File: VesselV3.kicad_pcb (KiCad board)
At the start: 2 copper layers, 0 parts

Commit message: PCB layout - Initial Commit
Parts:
- added BuckConverter1v8: TPS6285010MQDRLRQ1, SamacSys_Parts:SOTFL50P160X60-8N, F.Cu at (281.0, 51.8)
- added BuckConverter3v3: AP63203WU-7, SamacSys_Parts:SOT95P280X100-6N, F.Cu at (235.4, 45.8)
- added C1: 20pF, SamacSys_Parts:C0805, F.Cu at (199.1, 56.1)
- added C10: 4.7u, SamacSys_Parts:C0805, F.Cu at (378.3, 112.7)
- added C11: 4.7u, SamacSys_Parts:C0805, F.Cu at (378.3, 134.5)
- added C12: 4.7u, SamacSys_Parts:C0805, F.Cu at (378.3, 153.4)
- added C13: 4.7u, SamacSys_Parts:C0805, F.Cu at (378.3, 172.5)
- added C14: 4.7u, SamacSys_Parts:C0805, F.Cu at (378.3, 191.5)
- added C15: 4.7u, SamacSys_Parts:C0805, F.Cu at (354.8, 194.3)
- added C16: 2.2uF, SamacSys_Parts:CAPC1608X90N, F.Cu at (272.2, 65.8)
- added C17: 0.1uF, SamacSys_Parts:CAPC1005X55N, F.Cu at (265.8, 60.1)
- added C18: 4.7u, SamacSys_Parts:C0805, F.Cu at (342.7, 41.0)
- added C19: c=1e-05, SamacSys_Parts:CAPC2012X140N, F.Cu at (285.8, 49.3)
- added C2: 20pF, SamacSys_Parts:C0805, F.Cu at (213.3, 70.3)
- added C20: c=1e-05, SamacSys_Parts:CAPC2012X140N, F.Cu at (287.8, 49.3)
- added C21: 10pF, SamacSys_Parts:CAPC2012X75N, F.Cu at (277.1, 54.5)
- added C22: c=1e-05, SamacSys_Parts:CAPC2012X140N, F.Cu at (275.5, 59.2)
- added C23: c=1e-05, SamacSys_Parts:CAPC2012X140N, F.Cu at (279.0, 59.2)
- added C24: 0.1uF, SamacSys_Parts:CAPC1005X55N, F.Cu at (267.0, 60.1)
- added C25: 0.1uF, SamacSys_Parts:CAPC1005X55N, F.Cu at (211.0, 63.4)
- added C26: 0.1uF, SamacSys_Parts:CAPC1005X55N, F.Cu at (207.6, 52.3)
- added C27: 0.1uF, SamacSys_Parts:CAPC1005X55N, F.Cu at (227.0, 58.6)
- added C28: 0.1uF, SamacSys_Parts:CAPC1005X55N, F.Cu at (219.1, 46.4)
- added C29: 4.7u, SamacSys_Parts:C0805, F.Cu at (224.3, 61.2)
- added C3: 0.1u, SamacSys_Parts:C0805, F.Cu at (202.4, 52.2)
- added C30: 0.1uF, SamacSys_Parts:CAPC1005X55N, F.Cu at (210.3, 61.1)
- added C31: 0.1uF, SamacSys_Parts:CAPC1005X55N, F.Cu at (221.4, 64.0)
- added C32: 0.1uF, SamacSys_Parts:CAPC1005X55N, F.Cu at (299.7, 50.0)
- added C33: c=1e-05, SamacSys_Parts:CAPC2012X140N, F.Cu at (293.1, 51.9)
- added C34: 0.1uF, SamacSys_Parts:CAPC1005X55N, F.Cu at (272.2, 63.6)
- added C35: 2.2uF, SamacSys_Parts:CAPC1608X90N, F.Cu at (281.8, 64.1)
- added C36: 0.01u, SamacSys_Parts:CAPC1005X56N, F.Cu at (201.0, 41.3)
- added C37: 0.01u, SamacSys_Parts:CAPC1005X56N, F.Cu at (200.2, 42.1)
- added C38: 0.1uF, SamacSys_Parts:CAPC1005X55N, F.Cu at (204.8, 49.8)
- added C39: 0.1uF, SamacSys_Parts:CAPC1005X55N, F.Cu at (200.5, 45.5)
- added C4: c=2.2e-05, SamacSys_Parts:CAPC2012X95N, F.Cu at (236.7, 59.6)
- added C40: 0.1uF, SamacSys_Parts:CAPC1005X55N, F.Cu at (268.2, 60.1)
- added C41: 0.01u, SamacSys_Parts:CAPC1005X56N, F.Cu at (201.8, 40.7)
- added C5: c=2.2e-05, SamacSys_Parts:CAPC2012X95N, F.Cu at (236.7, 61.6)
- added C6: c=1e-07, SamacSys_Parts:CAPC2012X95N, F.Cu at (236.0, 50.9)
- added C7: c=1e-05, SamacSys_Parts:CAPC2012X140N, F.Cu at (235.1, 42.2)
- added C8: 0.1u, SamacSys_Parts:C0805, F.Cu at (220.8, 39.4)
- added C9: 4.7u, SamacSys_Parts:C0805, F.Cu at (378.3, 90.8)
- added D1: D_Small, SamacSys_Parts:SODFL3816X120N, B.Cu at (62.5, 90.5)
- added D10: D_Small, SamacSys_Parts:SODFL3816X120N, B.Cu at (253.0, 90.5)
- added D100: D_Small, SamacSys_Parts:SODFL3816X120N, B.Cu at (310.2, 210.5)
- added D101: D_Small, SamacSys_Parts:SODFL3816X120N, B.Cu at (329.2, 210.5)
- added D102: D_Small, SamacSys_Parts:SODFL3816X120N, B.Cu at (348.3, 210.5)
- added D11: D_Small, SamacSys_Parts:SODFL3816X120N, B.Cu at (276.9, 90.5)
- added D12: D_Small, SamacSys_Parts:SODFL3816X120N, B.Cu at (295.9, 90.5)
- added D13: D_Small, SamacSys_Parts:SODFL3816X120N, B.Cu at (334.0, 90.5)
- added D14: D_Small, SamacSys_Parts:SODFL3816X120N, B.Cu at (353.1, 90.5)
- added D15: D_Small, SamacSys_Parts:SODFL3816X120N, B.Cu at (372.1, 90.5)
- added D16: D_Small, SamacSys_Parts:SODFL3816X120N, B.Cu at (62.5, 112.4)
- added D17: D_Small, SamacSys_Parts:SODFL3816X120N, B.Cu at (91.1, 112.4)
- added D18: D_Small, SamacSys_Parts:SODFL3816X120N, B.Cu at (110.2, 112.4)
- added D19: D_Small, SamacSys_Parts:SODFL3816X120N, B.Cu at (129.2, 112.4)
- added D2: D_Small, SamacSys_Parts:SODFL3816X120N, B.Cu at (81.6, 90.5)
- added D20: D_Small, SamacSys_Parts:SODFL3816X120N, B.Cu at (148.3, 112.4)
- added D21: D_Small, SamacSys_Parts:SODFL3816X120N, B.Cu at (172.1, 112.4)
- added D22: D_Small, SamacSys_Parts:SODFL3816X120N, B.Cu at (191.1, 112.4)
- added D23: D_Small, SamacSys_Parts:SODFL3816X120N, B.Cu at (210.2, 112.4)
- added D24: D_Small, SamacSys_Parts:SODFL3816X120N, B.Cu at (229.2, 112.4)
- added D25: D_Small, SamacSys_Parts:SODFL3816X120N, B.Cu at (253.0, 112.4)
- added D26: D_Small, SamacSys_Parts:SODFL3816X120N, B.Cu at (272.1, 112.4)
- added D27: D_Small, SamacSys_Parts:SODFL3816X120N, B.Cu at (291.1, 112.4)
- added D28: D_Small, SamacSys_Parts:SODFL3816X120N, B.Cu at (310.2, 112.4)
- added D29: D_Small, SamacSys_Parts:SODFL3816X120N, B.Cu at (334.0, 112.4)
- added D3: D_Small, SamacSys_Parts:SODFL3816X120N, B.Cu at (105.4, 90.5)
- added D30: D_Small, SamacSys_Parts:SODFL3816X120N, B.Cu at (353.1, 112.4)
- added D31: D_Small, SamacSys_Parts:SODFL3816X120N, B.Cu at (372.1, 112.4)
- added D32: D_Small, SamacSys_Parts:SODFL3816X120N, B.Cu at (62.5, 134.3)
- added D33: D_Small, SamacSys_Parts:SODFL3816X120N, B.Cu at (81.6, 134.3)
- added D34: D_Small, SamacSys_Parts:SODFL3816X120N, B.Cu at (100.6, 134.3)
- added D35: D_Small, SamacSys_Parts:SODFL3816X120N, B.Cu at (119.7, 134.3)
- added D36: D_Small, SamacSys_Parts:SODFL3816X120N, B.Cu at (138.7, 134.3)
- added D37: D_Small, SamacSys_Parts:SODFL3816X120N, B.Cu at (157.8, 134.3)
- added D38: D_Small, SamacSys_Parts:SODFL3816X120N, B.Cu at (176.8, 134.3)
- added D39: D_Small, SamacSys_Parts:SODFL3816X120N, B.Cu at (195.9, 134.3)
- added D4: D_Small, SamacSys_Parts:SODFL3816X120N, B.Cu at (124.5, 90.5)
- added D40: D_Small, SamacSys_Parts:SODFL3816X120N, B.Cu at (214.9, 134.3)
- added D41: D_Small, SamacSys_Parts:SODFL3816X120N, B.Cu at (234.0, 134.3)
- added D42: D_Small, SamacSys_Parts:SODFL3816X120N, B.Cu at (253.0, 134.3)
- added D43: D_Small, SamacSys_Parts:SODFL3816X120N, B.Cu at (272.1, 134.3)
- added D44: D_Small, SamacSys_Parts:SODFL3816X120N, B.Cu at (291.1, 134.3)
- added D45: D_Small, SamacSys_Parts:SODFL3816X120N, B.Cu at (319.7, 134.3)
- added D46: D_Small, SamacSys_Parts:SODFL3816X120N, B.Cu at (353.1, 134.3)
- added D47: D_Small, SamacSys_Parts:SODFL3816X120N, B.Cu at (372.1, 134.3)
- added D48: D_Small, SamacSys_Parts:SODFL3816X120N, B.Cu at (67.3, 153.3)
- added D49: D_Small, SamacSys_Parts:SODFL3816X120N, B.Cu at (91.1, 153.3)
- added D5: D_Small, SamacSys_Parts:SODFL3816X120N, B.Cu at (148.3, 90.5)
- added D50: D_Small, SamacSys_Parts:SODFL3816X120N, B.Cu at (110.2, 153.3)
- added D51: D_Small, SamacSys_Parts:SODFL3816X120N, B.Cu at (129.2, 153.3)
- added D52: D_Small, SamacSys_Parts:SODFL3816X120N, B.Cu at (148.3, 153.3)
- added D53: D_Small, SamacSys_Parts:SODFL3816X120N, B.Cu at (167.3, 153.3)
- added D54: D_Small, SamacSys_Parts:SODFL3816X120N, B.Cu at (186.4, 153.3)
- added D55: D_Small, SamacSys_Parts:SODFL3816X120N, B.Cu at (205.4, 153.3)
- added D56: D_Small, SamacSys_Parts:SODFL3816X120N, B.Cu at (224.5, 153.3)
- added D57: D_Small, SamacSys_Parts:SODFL3816X120N, B.Cu at (243.5, 153.3)
- added D58: D_Small, SamacSys_Parts:SODFL3816X120N, B.Cu at (262.6, 153.3)
- added D59: D_Small, SamacSys_Parts:SODFL3816X120N, B.Cu at (281.6, 153.3)
- added D6: D_Small, SamacSys_Parts:SODFL3816X120N, B.Cu at (167.3, 90.5)
- added D60: D_Small, SamacSys_Parts:SODFL3816X120N, B.Cu at (300.7, 153.3)
- added D61: D_Small, SamacSys_Parts:SODFL3816X120N, B.Cu at (326.9, 162.8)
- added D62: D_Small, SamacSys_Parts:SODFL3816X120N, B.Cu at (353.1, 153.3)
- added D63: D_Small, SamacSys_Parts:SODFL3816X120N, B.Cu at (372.1, 153.3)
- added D64: D_Small, SamacSys_Parts:SODFL3816X120N, B.Cu at (69.7, 172.4)
- added D65: D_Small, SamacSys_Parts:SODFL3816X120N, B.Cu at (95.9, 172.4)
- added D66: D_Small, SamacSys_Parts:SODFL3816X120N, B.Cu at (114.9, 172.4)
- added D67: D_Small, SamacSys_Parts:SODFL3816X120N, B.Cu at (134.0, 172.4)
- added D68: D_Small, SamacSys_Parts:SODFL3816X120N, B.Cu at (153.0, 172.4)
- added D69: D_Small, SamacSys_Parts:SODFL3816X120N, B.Cu at (172.1, 172.4)
- added D7: D_Small, SamacSys_Parts:SODFL3816X120N, B.Cu at (191.1, 90.5)
- added D70: D_Small, SamacSys_Parts:SODFL3816X120N, B.Cu at (191.1, 172.4)
- added D71: D_Small, SamacSys_Parts:SODFL3816X120N, B.Cu at (210.2, 172.4)
- added D72: D_Small, SamacSys_Parts:SODFL3816X120N, B.Cu at (229.2, 172.4)
- added D73: D_Small, SamacSys_Parts:SODFL3816X120N, B.Cu at (248.3, 172.4)
- added D74: D_Small, SamacSys_Parts:SODFL3816X120N, B.Cu at (267.3, 172.4)
- added D75: D_Small, SamacSys_Parts:SODFL3816X120N, B.Cu at (286.4, 172.4)
- added D76: D_Small, SamacSys_Parts:SODFL3816X120N, B.Cu at (305.4, 172.4)
- added D77: D_Small, SamacSys_Parts:SODFL3816X120N, B.Cu at (353.1, 172.4)
- added D78: D_Small, SamacSys_Parts:SODFL3816X120N, B.Cu at (372.1, 172.4)
- added D79: D_Small, SamacSys_Parts:SODFL3816X120N, B.Cu at (64.9, 191.4)
- added D8: D_Small, SamacSys_Parts:SODFL3816X120N, B.Cu at (210.2, 90.5)
- added D80: D_Small, SamacSys_Parts:SODFL3816X120N, B.Cu at (86.4, 191.4)
- added D81: D_Small, SamacSys_Parts:SODFL3816X120N, B.Cu at (105.4, 191.4)
- added D82: D_Small, SamacSys_Parts:SODFL3816X120N, B.Cu at (124.5, 191.4)
- added D83: D_Small, SamacSys_Parts:SODFL3816X120N, B.Cu at (143.5, 191.4)
- added D84: D_Small, SamacSys_Parts:SODFL3816X120N, B.Cu at (162.6, 191.4)
- added D85: D_Small, SamacSys_Parts:SODFL3816X120N, B.Cu at (181.6, 191.4)
- added D86: D_Small, SamacSys_Parts:SODFL3816X120N, B.Cu at (200.7, 191.4)
- added D87: D_Small, SamacSys_Parts:SODFL3816X120N, B.Cu at (219.7, 191.4)
- added D88: D_Small, SamacSys_Parts:SODFL3816X120N, B.Cu at (238.8, 191.4)
- added D89: D_Small, SamacSys_Parts:SODFL3816X120N, B.Cu at (257.8, 191.4)
- added D9: D_Small, SamacSys_Parts:SODFL3816X120N, B.Cu at (234.0, 90.5)
- added D90: D_Small, SamacSys_Parts:SODFL3816X120N, B.Cu at (276.9, 191.4)
- added D91: D_Small, SamacSys_Parts:SODFL3816X120N, B.Cu at (303.1, 191.4)
- added D92: D_Small, SamacSys_Parts:SODFL3816X120N, B.Cu at (329.2, 191.4)
- added D93: D_Small, SamacSys_Parts:SODFL3816X120N, B.Cu at (372.1, 191.4)
- added D94: D_Small, SamacSys_Parts:SODFL3816X120N, B.Cu at (64.9, 210.5)
- added D95: D_Small, SamacSys_Parts:SODFL3816X120N, B.Cu at (88.7, 210.5)
- added D96: D_Small, SamacSys_Parts:SODFL3816X120N, B.Cu at (112.6, 210.5)
- added D97: D_Small, SamacSys_Parts:SODFL3816X120N, B.Cu at (184.0, 210.5)
- added D98: D_Small, SamacSys_Parts:SODFL3816X120N, B.Cu at (255.4, 210.5)
- added D99: D_Small, SamacSys_Parts:SODFL3816X120N, B.Cu at (279.2, 210.5)
- added IC1: USB3320C-EZK-TR, SamacSys_Parts:QFN50P500X500X100-33N-D, F.Cu at (267.6, 64.9)
- added IC3: 5VOutput_VoltageRegulator, SamacSys_Parts:TO228P972X240-3N, F.Cu at (297.7, 56.1)
- added IC4: BidirectionalLogicLevelShifter, SamacSys_Parts:SOP65P640X120-14N, F.Cu at (205.0, 45.2)
- added IC6: AND Gate, SamacSys_Parts:SOT65P212X110-5N, F.Cu at (226.7, 64.0)
- added Inductor1: 3.9uH, Inductor3.9uH:IND_LQH32NH3R9J23L, F.Cu at (236.3, 54.9)
- added J1: JTAG/SWD 10pins Headers, SamacSys_Parts:HUSSP10W40P127_2X5_635X340X420P, F.Cu at (210.1, 40.6)
- added JSTPH4-PIN1: 4392, SamacSys_Parts:4392, F.Cu at (323.6, 59.4)
- added L1: 0.47uH, SamacSys_Parts:INDC2012X105N, F.Cu at (277.1, 52.1)
- added LED1: 4684, WS2812BNano4684RGB-3rdParty:4684_ADA, F.Cu at (57.5, 92.4)
- added LED10: 4684, WS2812BNano4684RGB-3rdParty:4684_ADA, F.Cu at (248.0, 92.4)
- added LED100: 4684, WS2812BNano4684RGB-3rdParty:4684_ADA, F.Cu at (305.1, 212.4)
- added LED101: 4684, WS2812BNano4684RGB-3rdParty:4684_ADA, F.Cu at (324.2, 212.4)
- added LED102: 4684, WS2812BNano4684RGB-3rdParty:4684_ADA, F.Cu at (343.2, 212.4)
- added LED11: 4684, WS2812BNano4684RGB-3rdParty:4684_ADA, F.Cu at (271.8, 92.4)
- added LED12: 4684, WS2812BNano4684RGB-3rdParty:4684_ADA, F.Cu at (290.8, 92.4)
- added LED13: 4684, WS2812BNano4684RGB-3rdParty:4684_ADA, F.Cu at (328.9, 92.4)
- added LED14: 4684, WS2812BNano4684RGB-3rdParty:4684_ADA, F.Cu at (348.0, 92.4)
- added LED15: 4684, WS2812BNano4684RGB-3rdParty:4684_ADA, F.Cu at (367.0, 92.4)
- added LED16: 4684, WS2812BNano4684RGB-3rdParty:4684_ADA, F.Cu at (57.5, 114.3)
- added LED17: 4684, WS2812BNano4684RGB-3rdParty:4684_ADA, F.Cu at (86.0, 114.3)
- added LED18: 4684, WS2812BNano4684RGB-3rdParty:4684_ADA, F.Cu at (105.1, 114.3)
- added LED19: 4684, WS2812BNano4684RGB-3rdParty:4684_ADA, F.Cu at (124.1, 114.3)
- added LED2: 4684, WS2812BNano4684RGB-3rdParty:4684_ADA, F.Cu at (76.5, 92.4)
- added LED20: 4684, WS2812BNano4684RGB-3rdParty:4684_ADA, F.Cu at (143.2, 114.3)
- added LED21: 4684, WS2812BNano4684RGB-3rdParty:4684_ADA, F.Cu at (167.0, 114.3)
- added LED22: 4684, WS2812BNano4684RGB-3rdParty:4684_ADA, F.Cu at (186.1, 114.3)
- added LED23: 4684, WS2812BNano4684RGB-3rdParty:4684_ADA, F.Cu at (205.1, 114.3)
- added LED24: 4684, WS2812BNano4684RGB-3rdParty:4684_ADA, F.Cu at (224.2, 114.3)
- added LED25: 4684, WS2812BNano4684RGB-3rdParty:4684_ADA, F.Cu at (248.0, 114.3)
- added LED26: 4684, WS2812BNano4684RGB-3rdParty:4684_ADA, F.Cu at (267.0, 114.3)
- added LED27: 4684, WS2812BNano4684RGB-3rdParty:4684_ADA, F.Cu at (286.1, 114.3)
- added LED28: 4684, WS2812BNano4684RGB-3rdParty:4684_ADA, F.Cu at (305.1, 114.3)
- added LED29: 4684, WS2812BNano4684RGB-3rdParty:4684_ADA, F.Cu at (328.9, 114.3)
- added LED3: 4684, WS2812BNano4684RGB-3rdParty:4684_ADA, F.Cu at (100.3, 92.4)
- added LED30: 4684, WS2812BNano4684RGB-3rdParty:4684_ADA, F.Cu at (348.0, 114.3)
- added LED31: 4684, WS2812BNano4684RGB-3rdParty:4684_ADA, F.Cu at (367.0, 114.3)
- added LED32: 4684, WS2812BNano4684RGB-3rdParty:4684_ADA, F.Cu at (57.5, 136.2)
- added LED33: 4684, WS2812BNano4684RGB-3rdParty:4684_ADA, F.Cu at (76.5, 136.2)
- added LED34: 4684, WS2812BNano4684RGB-3rdParty:4684_ADA, F.Cu at (95.6, 136.2)
- added LED35: 4684, WS2812BNano4684RGB-3rdParty:4684_ADA, F.Cu at (114.6, 136.2)
- added LED36: 4684, WS2812BNano4684RGB-3rdParty:4684_ADA, F.Cu at (133.7, 136.2)
- added LED37: 4684, WS2812BNano4684RGB-3rdParty:4684_ADA, F.Cu at (152.7, 136.2)
- added LED38: 4684, WS2812BNano4684RGB-3rdParty:4684_ADA, F.Cu at (171.8, 136.2)
- added LED39: 4684, WS2812BNano4684RGB-3rdParty:4684_ADA, F.Cu at (190.8, 136.2)
- added LED4: 4684, WS2812BNano4684RGB-3rdParty:4684_ADA, F.Cu at (119.4, 92.4)
- added LED40: 4684, WS2812BNano4684RGB-3rdParty:4684_ADA, F.Cu at (209.9, 136.2)
- added LED41: 4684, WS2812BNano4684RGB-3rdParty:4684_ADA, F.Cu at (228.9, 136.2)
- added LED42: 4684, WS2812BNano4684RGB-3rdParty:4684_ADA, F.Cu at (248.0, 136.2)
- added LED43: 4684, WS2812BNano4684RGB-3rdParty:4684_ADA, F.Cu at (267.0, 136.2)
- added LED44: 4684, WS2812BNano4684RGB-3rdParty:4684_ADA, F.Cu at (286.1, 136.2)
- added LED45: 4684, WS2812BNano4684RGB-3rdParty:4684_ADA, F.Cu at (314.6, 136.2)
- added LED46: 4684, WS2812BNano4684RGB-3rdParty:4684_ADA, F.Cu at (348.0, 136.2)
- added LED47: 4684, WS2812BNano4684RGB-3rdParty:4684_ADA, F.Cu at (367.0, 136.2)
- added LED48: 4684, WS2812BNano4684RGB-3rdParty:4684_ADA, F.Cu at (62.2, 155.2)
- added LED49: 4684, WS2812BNano4684RGB-3rdParty:4684_ADA, F.Cu at (86.0, 155.2)
- added LED5: 4684, WS2812BNano4684RGB-3rdParty:4684_ADA, F.Cu at (143.2, 92.4)
- added LED50: 4684, WS2812BNano4684RGB-3rdParty:4684_ADA, F.Cu at (105.1, 155.2)
- added LED51: 4684, WS2812BNano4684RGB-3rdParty:4684_ADA, F.Cu at (124.1, 155.2)
- added LED52: 4684, WS2812BNano4684RGB-3rdParty:4684_ADA, F.Cu at (143.2, 155.2)
- added LED53: 4684, WS2812BNano4684RGB-3rdParty:4684_ADA, F.Cu at (162.2, 155.2)
- added LED54: 4684, WS2812BNano4684RGB-3rdParty:4684_ADA, F.Cu at (181.3, 155.2)
- added LED55: 4684, WS2812BNano4684RGB-3rdParty:4684_ADA, F.Cu at (200.3, 155.2)
- added LED56: 4684, WS2812BNano4684RGB-3rdParty:4684_ADA, F.Cu at (219.4, 155.2)
- added LED57: 4684, WS2812BNano4684RGB-3rdParty:4684_ADA, F.Cu at (238.4, 155.2)
- added LED58: 4684, WS2812BNano4684RGB-3rdParty:4684_ADA, F.Cu at (257.5, 155.2)
- added LED59: 4684, WS2812BNano4684RGB-3rdParty:4684_ADA, F.Cu at (276.5, 155.2)
- added LED6: 4684, WS2812BNano4684RGB-3rdParty:4684_ADA, F.Cu at (162.2, 92.4)
- added LED60: 4684, WS2812BNano4684RGB-3rdParty:4684_ADA, F.Cu at (295.6, 155.2)
- added LED61: 4684, WS2812BNano4684RGB-3rdParty:4684_ADA, F.Cu at (321.8, 164.7)
- added LED62: 4684, WS2812BNano4684RGB-3rdParty:4684_ADA, F.Cu at (348.0, 155.2)
- added LED63: 4684, WS2812BNano4684RGB-3rdParty:4684_ADA, F.Cu at (367.0, 155.2)
- added LED64: 4684, WS2812BNano4684RGB-3rdParty:4684_ADA, F.Cu at (64.6, 174.3)
- added LED65: 4684, WS2812BNano4684RGB-3rdParty:4684_ADA, F.Cu at (90.8, 174.3)
- added LED66: 4684, WS2812BNano4684RGB-3rdParty:4684_ADA, F.Cu at (109.9, 174.3)
- added LED67: 4684, WS2812BNano4684RGB-3rdParty:4684_ADA, F.Cu at (128.9, 174.3)
- added LED68: 4684, WS2812BNano4684RGB-3rdParty:4684_ADA, F.Cu at (148.0, 174.3)
- added LED69: 4684, WS2812BNano4684RGB-3rdParty:4684_ADA, F.Cu at (167.0, 174.3)
- added LED7: 4684, WS2812BNano4684RGB-3rdParty:4684_ADA, F.Cu at (186.1, 92.4)
- added LED70: 4684, WS2812BNano4684RGB-3rdParty:4684_ADA, F.Cu at (186.1, 174.3)
- added LED71: 4684, WS2812BNano4684RGB-3rdParty:4684_ADA, F.Cu at (205.1, 174.3)
- added LED72: 4684, WS2812BNano4684RGB-3rdParty:4684_ADA, F.Cu at (224.2, 174.3)
- added LED73: 4684, WS2812BNano4684RGB-3rdParty:4684_ADA, F.Cu at (243.2, 174.3)
- added LED74: 4684, WS2812BNano4684RGB-3rdParty:4684_ADA, F.Cu at (262.3, 174.3)
- added LED75: 4684, WS2812BNano4684RGB-3rdParty:4684_ADA, F.Cu at (281.3, 174.3)
- added LED76: 4684, WS2812BNano4684RGB-3rdParty:4684_ADA, F.Cu at (300.4, 174.3)
- added LED77: 4684, WS2812BNano4684RGB-3rdParty:4684_ADA, F.Cu at (348.0, 174.3)
- added LED78: 4684, WS2812BNano4684RGB-3rdParty:4684_ADA, F.Cu at (367.0, 174.3)
- added LED79: 4684, WS2812BNano4684RGB-3rdParty:4684_ADA, F.Cu at (59.8, 193.3)
- added LED8: 4684, WS2812BNano4684RGB-3rdParty:4684_ADA, F.Cu at (205.1, 92.4)
- added LED80: 4684, WS2812BNano4684RGB-3rdParty:4684_ADA, F.Cu at (81.3, 193.3)
- added LED81: 4684, WS2812BNano4684RGB-3rdParty:4684_ADA, F.Cu at (100.3, 193.3)
- added LED82: 4684, WS2812BNano4684RGB-3rdParty:4684_ADA, F.Cu at (119.4, 193.3)
- added LED83: 4684, WS2812BNano4684RGB-3rdParty:4684_ADA, F.Cu at (138.4, 193.3)
- added LED84: 4684, WS2812BNano4684RGB-3rdParty:4684_ADA, F.Cu at (157.5, 193.3)
- added LED85: 4684, WS2812BNano4684RGB-3rdParty:4684_ADA, F.Cu at (176.5, 193.3)
- added LED86: 4684, WS2812BNano4684RGB-3rdParty:4684_ADA, F.Cu at (195.6, 193.3)
- added LED87: 4684, WS2812BNano4684RGB-3rdParty:4684_ADA, F.Cu at (214.6, 193.3)
- added LED88: 4684, WS2812BNano4684RGB-3rdParty:4684_ADA, F.Cu at (233.7, 193.3)
- added LED89: 4684, WS2812BNano4684RGB-3rdParty:4684_ADA, F.Cu at (252.7, 193.3)
- added LED9: 4684, WS2812BNano4684RGB-3rdParty:4684_ADA, F.Cu at (228.9, 92.4)
- added LED90: 4684, WS2812BNano4684RGB-3rdParty:4684_ADA, F.Cu at (271.8, 193.3)
- added LED91: 4684, WS2812BNano4684RGB-3rdParty:4684_ADA, F.Cu at (298.0, 193.3)
- added LED92: 4684, WS2812BNano4684RGB-3rdParty:4684_ADA, F.Cu at (324.2, 193.3)
- added LED93: 4684, WS2812BNano4684RGB-3rdParty:4684_ADA, F.Cu at (367.0, 193.3)
- added LED94: 4684, WS2812BNano4684RGB-3rdParty:4684_ADA, F.Cu at (59.8, 212.4)
- added LED95: 4684, WS2812BNano4684RGB-3rdParty:4684_ADA, F.Cu at (83.7, 212.4)
- added LED96: 4684, WS2812BNano4684RGB-3rdParty:4684_ADA, F.Cu at (107.5, 212.4)
- added LED97: 4684, WS2812BNano4684RGB-3rdParty:4684_ADA, F.Cu at (178.9, 212.4)
- added LED98: 4684, WS2812BNano4684RGB-3rdParty:4684_ADA, F.Cu at (250.3, 212.4)
- added LED99: 4684, WS2812BNano4684RGB-3rdParty:4684_ADA, F.Cu at (274.2, 212.4)
- added MCU1: STM32F446RET6TR, SamacSys_Parts:QFP50P1200X1200X160-64N, F.Cu at (216.0, 54.2)
- added MX1: MX_SW_solder, PCM_Switch_Keyboard_Cherry_MX:SW_Cherry_MX_PCB_1.00u, F.Cu at (57.5, 87.2)
- added MX10: MX_SW_solder, PCM_Switch_Keyboard_Cherry_MX:SW_Cherry_MX_PCB_1.00u, F.Cu at (248.0, 87.2)
- added MX100: MX_SW_solder, PCM_Switch_Keyboard_Cherry_MX:SW_Cherry_MX_PCB_1.00u, F.Cu at (305.1, 207.2)
- added MX101: MX_SW_solder, PCM_Switch_Keyboard_Cherry_MX:SW_Cherry_MX_PCB_1.00u, F.Cu at (324.2, 207.2)
- added MX102: MX_SW_solder, PCM_Switch_Keyboard_Cherry_MX:SW_Cherry_MX_PCB_1.00u, F.Cu at (343.2, 207.2)
- added MX11: MX_SW_solder, PCM_Switch_Keyboard_Cherry_MX:SW_Cherry_MX_PCB_1.00u, F.Cu at (271.8, 87.2)
- added MX12: MX_SW_solder, PCM_Switch_Keyboard_Cherry_MX:SW_Cherry_MX_PCB_1.00u, F.Cu at (290.8, 87.2)
- added MX13: MX_SW_solder, PCM_Switch_Keyboard_Cherry_MX:SW_Cherry_MX_PCB_1.00u, F.Cu at (328.9, 87.2)
- added MX14: MX_SW_solder, PCM_Switch_Keyboard_Cherry_MX:SW_Cherry_MX_PCB_1.00u, F.Cu at (348.0, 87.2)
- added MX15: MX_SW_solder, PCM_Switch_Keyboard_Cherry_MX:SW_Cherry_MX_PCB_1.00u, F.Cu at (367.0, 87.2)
- added MX16: MX_SW_solder, PCM_Switch_Keyboard_Cherry_MX:SW_Cherry_MX_PCB_1.00u, F.Cu at (57.5, 109.1)
- added MX17: MX_SW_solder, PCM_Switch_Keyboard_Cherry_MX:SW_Cherry_MX_PCB_1.00u, F.Cu at (86.0, 109.1)
- added MX18: MX_SW_solder, PCM_Switch_Keyboard_Cherry_MX:SW_Cherry_MX_PCB_1.00u, F.Cu at (105.1, 109.1)
- added MX19: MX_SW_solder, PCM_Switch_Keyboard_Cherry_MX:SW_Cherry_MX_PCB_1.00u, F.Cu at (124.1, 109.1)
- added MX2: MX_SW_solder, PCM_Switch_Keyboard_Cherry_MX:SW_Cherry_MX_PCB_1.00u, F.Cu at (76.5, 87.2)
- added MX20: MX_SW_solder, PCM_Switch_Keyboard_Cherry_MX:SW_Cherry_MX_PCB_1.00u, F.Cu at (143.2, 109.1)
- added MX21: MX_SW_solder, PCM_Switch_Keyboard_Cherry_MX:SW_Cherry_MX_PCB_1.00u, F.Cu at (167.0, 109.1)
- added MX22: MX_SW_solder, PCM_Switch_Keyboard_Cherry_MX:SW_Cherry_MX_PCB_1.00u, F.Cu at (186.1, 109.1)
- added MX23: MX_SW_solder, PCM_Switch_Keyboard_Cherry_MX:SW_Cherry_MX_PCB_1.00u, F.Cu at (205.1, 109.1)
- added MX24: MX_SW_solder, PCM_Switch_Keyboard_Cherry_MX:SW_Cherry_MX_PCB_1.00u, F.Cu at (224.2, 109.1)
- added MX25: MX_SW_solder, PCM_Switch_Keyboard_Cherry_MX:SW_Cherry_MX_PCB_1.00u, F.Cu at (248.0, 109.1)
- added MX26: MX_SW_solder, PCM_Switch_Keyboard_Cherry_MX:SW_Cherry_MX_PCB_1.00u, F.Cu at (267.0, 109.1)
- added MX27: MX_SW_solder, PCM_Switch_Keyboard_Cherry_MX:SW_Cherry_MX_PCB_1.00u, F.Cu at (286.1, 109.1)
- added MX28: MX_SW_solder, PCM_Switch_Keyboard_Cherry_MX:SW_Cherry_MX_PCB_1.00u, F.Cu at (305.1, 109.1)
- added MX29: MX_SW_solder, PCM_Switch_Keyboard_Cherry_MX:SW_Cherry_MX_PCB_1.00u, F.Cu at (328.9, 109.1)
- added MX3: MX_SW_solder, PCM_Switch_Keyboard_Cherry_MX:SW_Cherry_MX_PCB_1.00u, F.Cu at (100.3, 87.2)
- added MX30: MX_SW_solder, PCM_Switch_Keyboard_Cherry_MX:SW_Cherry_MX_PCB_1.00u, F.Cu at (348.0, 109.1)
- added MX31: MX_SW_solder, PCM_Switch_Keyboard_Cherry_MX:SW_Cherry_MX_PCB_1.00u, F.Cu at (367.0, 109.1)
- added MX32: MX_SW_solder, PCM_Switch_Keyboard_Cherry_MX:SW_Cherry_MX_PCB_1.00u, F.Cu at (57.5, 131.0)
- added MX33: MX_SW_solder, PCM_Switch_Keyboard_Cherry_MX:SW_Cherry_MX_PCB_1.00u, F.Cu at (76.5, 131.0)
- added MX34: MX_SW_solder, PCM_Switch_Keyboard_Cherry_MX:SW_Cherry_MX_PCB_1.00u, F.Cu at (95.6, 131.0)
- added MX35: MX_SW_solder, PCM_Switch_Keyboard_Cherry_MX:SW_Cherry_MX_PCB_1.00u, F.Cu at (114.6, 131.0)
- added MX36: MX_SW_solder, PCM_Switch_Keyboard_Cherry_MX:SW_Cherry_MX_PCB_1.00u, F.Cu at (133.7, 131.0)
- added MX37: MX_SW_solder, PCM_Switch_Keyboard_Cherry_MX:SW_Cherry_MX_PCB_1.00u, F.Cu at (152.7, 131.0)
- added MX38: MX_SW_solder, PCM_Switch_Keyboard_Cherry_MX:SW_Cherry_MX_PCB_1.00u, F.Cu at (171.8, 131.0)
- added MX39: MX_SW_solder, PCM_Switch_Keyboard_Cherry_MX:SW_Cherry_MX_PCB_1.00u, F.Cu at (190.8, 131.0)
- added MX4: MX_SW_solder, PCM_Switch_Keyboard_Cherry_MX:SW_Cherry_MX_PCB_1.00u, F.Cu at (119.4, 87.2)
- added MX40: MX_SW_solder, PCM_Switch_Keyboard_Cherry_MX:SW_Cherry_MX_PCB_1.00u, F.Cu at (209.9, 131.0)
- added MX41: MX_SW_solder, PCM_Switch_Keyboard_Cherry_MX:SW_Cherry_MX_PCB_1.00u, F.Cu at (228.9, 131.0)
- added MX42: MX_SW_solder, PCM_Switch_Keyboard_Cherry_MX:SW_Cherry_MX_PCB_1.00u, F.Cu at (248.0, 131.0)
- added MX43: MX_SW_solder, PCM_Switch_Keyboard_Cherry_MX:SW_Cherry_MX_PCB_1.00u, F.Cu at (267.0, 131.0)
- added MX44: MX_SW_solder, PCM_Switch_Keyboard_Cherry_MX:SW_Cherry_MX_PCB_1.00u, F.Cu at (286.1, 131.0)
- added MX45: MX_SW_solder, PCM_Switch_Keyboard_Cherry_MX:SW_Cherry_MX_PCB_2.00u, F.Cu at (314.6, 131.0)
- added MX46: MX_SW_solder, PCM_Switch_Keyboard_Cherry_MX:SW_Cherry_MX_PCB_1.00u, F.Cu at (348.0, 131.0)
- added MX47: MX_SW_solder, PCM_Switch_Keyboard_Cherry_MX:SW_Cherry_MX_PCB_1.00u, F.Cu at (367.0, 131.0)
- added MX48: MX_SW_solder, PCM_Switch_Keyboard_Cherry_MX:SW_Cherry_MX_PCB_1.50u, F.Cu at (62.2, 150.0)
- added MX49: MX_SW_solder, PCM_Switch_Keyboard_Cherry_MX:SW_Cherry_MX_PCB_1.00u, F.Cu at (86.0, 150.0)
- added MX5: MX_SW_solder, PCM_Switch_Keyboard_Cherry_MX:SW_Cherry_MX_PCB_1.00u, F.Cu at (143.2, 87.2)
- added MX50: MX_SW_solder, PCM_Switch_Keyboard_Cherry_MX:SW_Cherry_MX_PCB_1.00u, F.Cu at (105.1, 150.0)
- added MX51: MX_SW_solder, PCM_Switch_Keyboard_Cherry_MX:SW_Cherry_MX_PCB_1.00u, F.Cu at (124.1, 150.0)
- added MX52: MX_SW_solder, PCM_Switch_Keyboard_Cherry_MX:SW_Cherry_MX_PCB_1.00u, F.Cu at (143.2, 150.0)
- added MX53: MX_SW_solder, PCM_Switch_Keyboard_Cherry_MX:SW_Cherry_MX_PCB_1.00u, F.Cu at (162.2, 150.0)
- added MX54: MX_SW_solder, PCM_Switch_Keyboard_Cherry_MX:SW_Cherry_MX_PCB_1.00u, F.Cu at (181.3, 150.0)
- added MX55: MX_SW_solder, PCM_Switch_Keyboard_Cherry_MX:SW_Cherry_MX_PCB_1.00u, F.Cu at (200.3, 150.0)
- added MX56: MX_SW_solder, PCM_Switch_Keyboard_Cherry_MX:SW_Cherry_MX_PCB_1.00u, F.Cu at (219.4, 150.0)
- added MX57: MX_SW_solder, PCM_Switch_Keyboard_Cherry_MX:SW_Cherry_MX_PCB_1.00u, F.Cu at (238.4, 150.0)
- added MX58: MX_SW_solder, PCM_Switch_Keyboard_Cherry_MX:SW_Cherry_MX_PCB_1.00u, F.Cu at (257.5, 150.0)
- added MX59: MX_SW_solder, PCM_Switch_Keyboard_Cherry_MX:SW_Cherry_MX_PCB_1.00u, F.Cu at (276.5, 150.0)
- added MX6: MX_SW_solder, PCM_Switch_Keyboard_Cherry_MX:SW_Cherry_MX_PCB_1.00u, F.Cu at (162.2, 87.2)
- added MX60: MX_SW_solder, PCM_Switch_Keyboard_Cherry_MX:SW_Cherry_MX_PCB_1.00u, F.Cu at (295.6, 150.0)
- added MX61: MX_SW_solder, PCM_Switch_Keyboard_Cherry_MX:SW_Cherry_MX_PCB_ISOEnter, F.Cu at (321.8, 159.5)
- added MX62: MX_SW_solder, PCM_Switch_Keyboard_Cherry_MX:SW_Cherry_MX_PCB_1.00u, F.Cu at (348.0, 150.0)
- added MX63: MX_SW_solder, PCM_Switch_Keyboard_Cherry_MX:SW_Cherry_MX_PCB_1.00u, F.Cu at (367.0, 150.0)
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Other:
- board outline added: 341.8 x 195.5 mm

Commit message: Rough PCB Layout and GPIO Pins Swaps
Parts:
- added C42: 0.1uF, SamacSys_Parts:CAPC1005X55N, F.Cu at (377.2, 94.1)
- moved BuckConverter3v3 4.98 mm to (230.4, 45.7)
- moved C6 4.98 mm to (231.0, 50.9)
- moved C7 4.98 mm to (230.2, 42.1)
- moved C3 2.13 mm to (200.5, 51.3)
- moved C36 2.13 mm to (199.1, 40.4)
- moved C37 2.13 mm to (198.3, 41.2)
- moved C38 2.13 mm to (202.9, 48.9)
- moved J1 2.13 mm to (208.2, 39.7)
- moved C1 2.13 mm to (197.1, 55.1)
- moved C39 2.13 mm to (198.6, 44.6)
- moved C41 2.13 mm to (199.8, 39.7)
- moved C8 2.13 mm to (218.9, 38.5)
- moved IC4 2.13 mm to (203.1, 44.3)
- moved PNPTransistor1 2.13 mm to (196.7, 48.0)
- moved R11 2.13 mm to (212.4, 42.0)
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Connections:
- MCU1 pad 15: ROW2 -> COL6
- MCU1 pad 16: ROW3 -> COL7
- MCU1 pad 22: ROW4 -> ROW0
- MCU1 pad 24: ROW6 -> ROW4
- MCU1 pad 25: COL0 -> ROW6
- MCU1 pad 3: ROW0 -> COL1
- MCU1 pad 35: COL1 -> ROW1
- MCU1 pad 36: COL2 -> ROW3
- MCU1 pad 39: COL3 -> ROW2
- MCU1 pad 40: COL4 -> COL14
- MCU1 pad 41: COL5 -> COL13
- MCU1 pad 42: COL6 -> COL12
- MCU1 pad 44: COL7 -> COL15
- MCU1 pad 45: COL8 -> COL16
- MCU1 pad 51: COL9 -> COL11
- MCU1 pad 53: COL11 -> COL9
- MCU1 pad 54: COL12 -> COL8
- MCU1 pad 58: COL13 -> COL0
- MCU1 pad 59: COL14 -> COL2
- MCU1 pad 61: COL15 -> COL3
- MCU1 pad 62: COL16 -> COL5
- MCU1 pad 9: ROW1 -> COL4
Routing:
- added copper zone on F.Cu, net GND

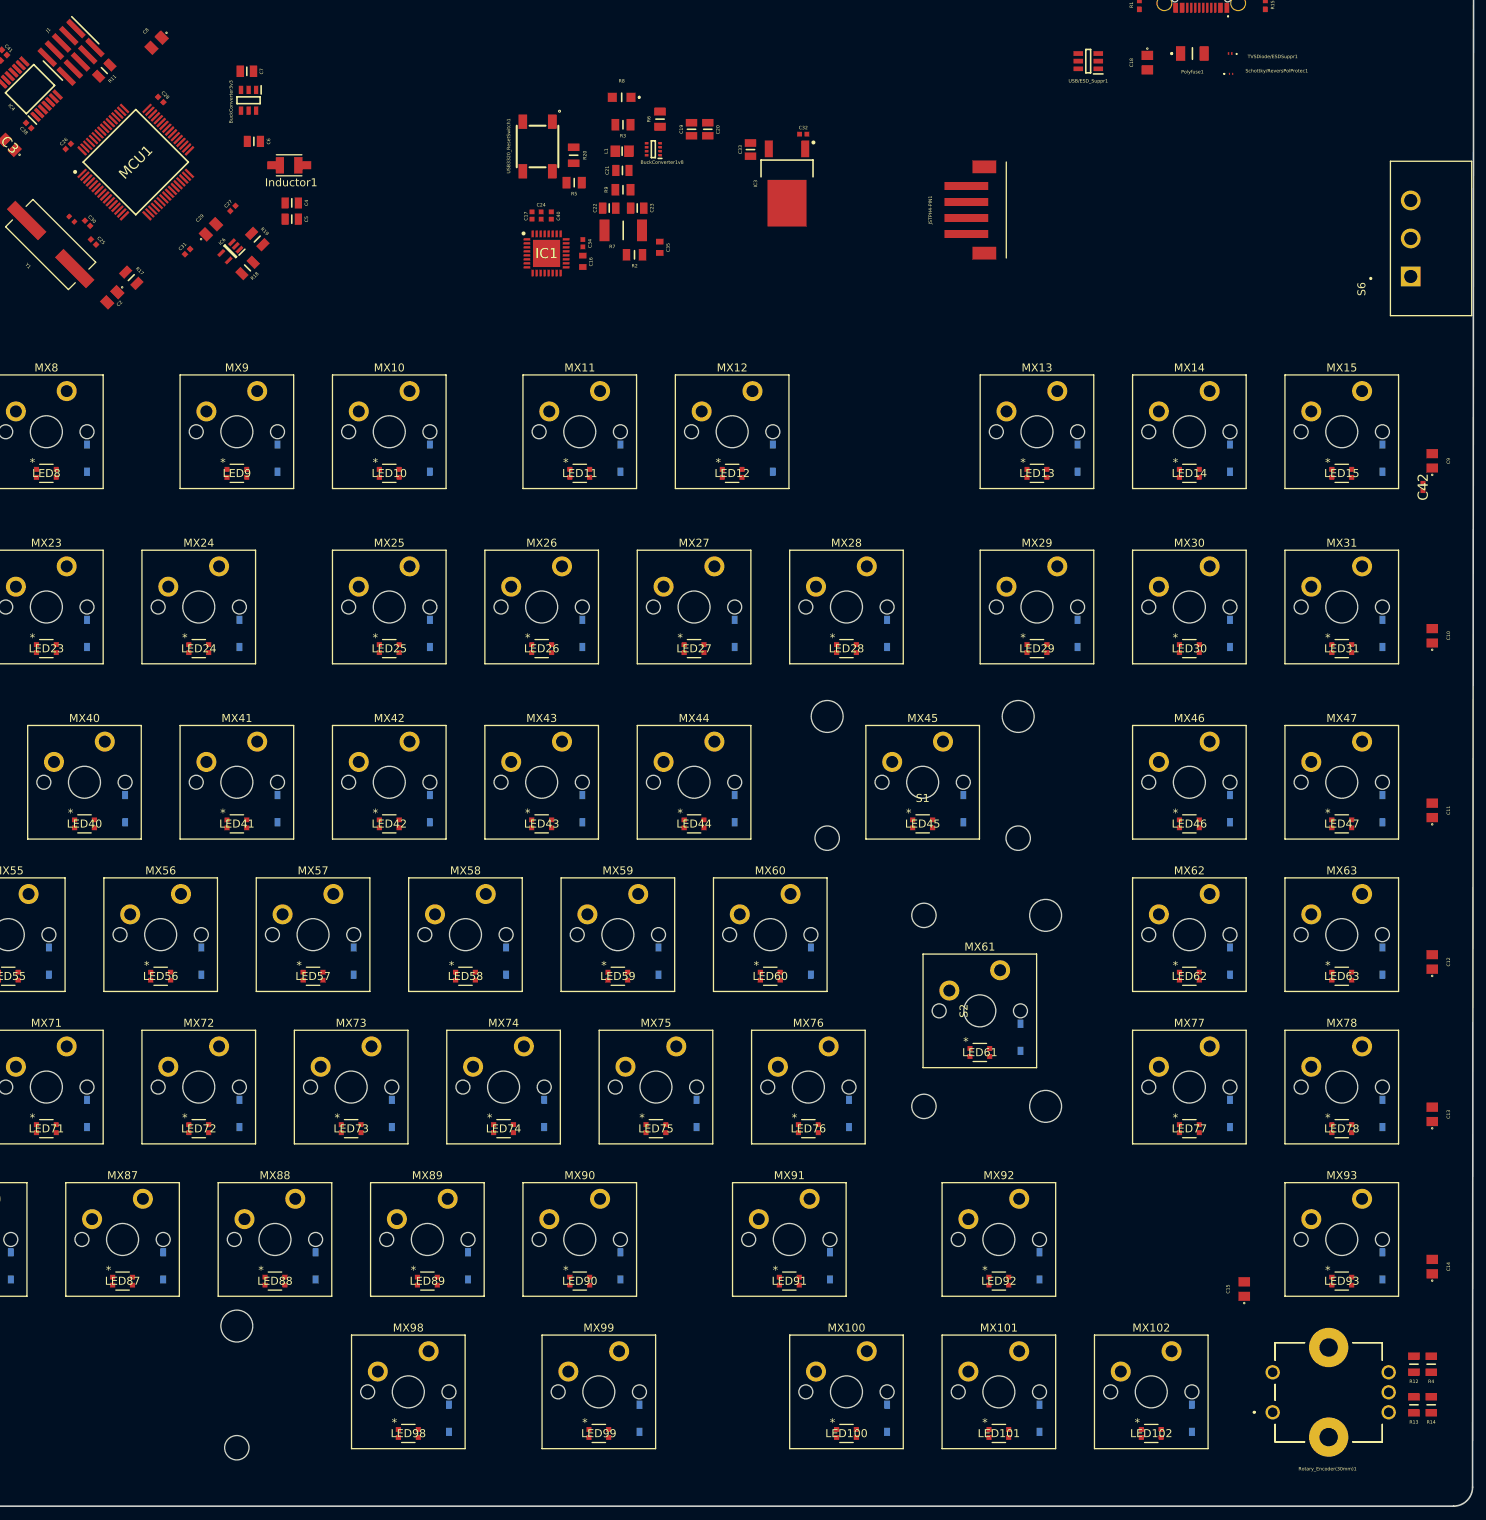
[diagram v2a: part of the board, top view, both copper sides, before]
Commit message: Swapped encoder for smaller one
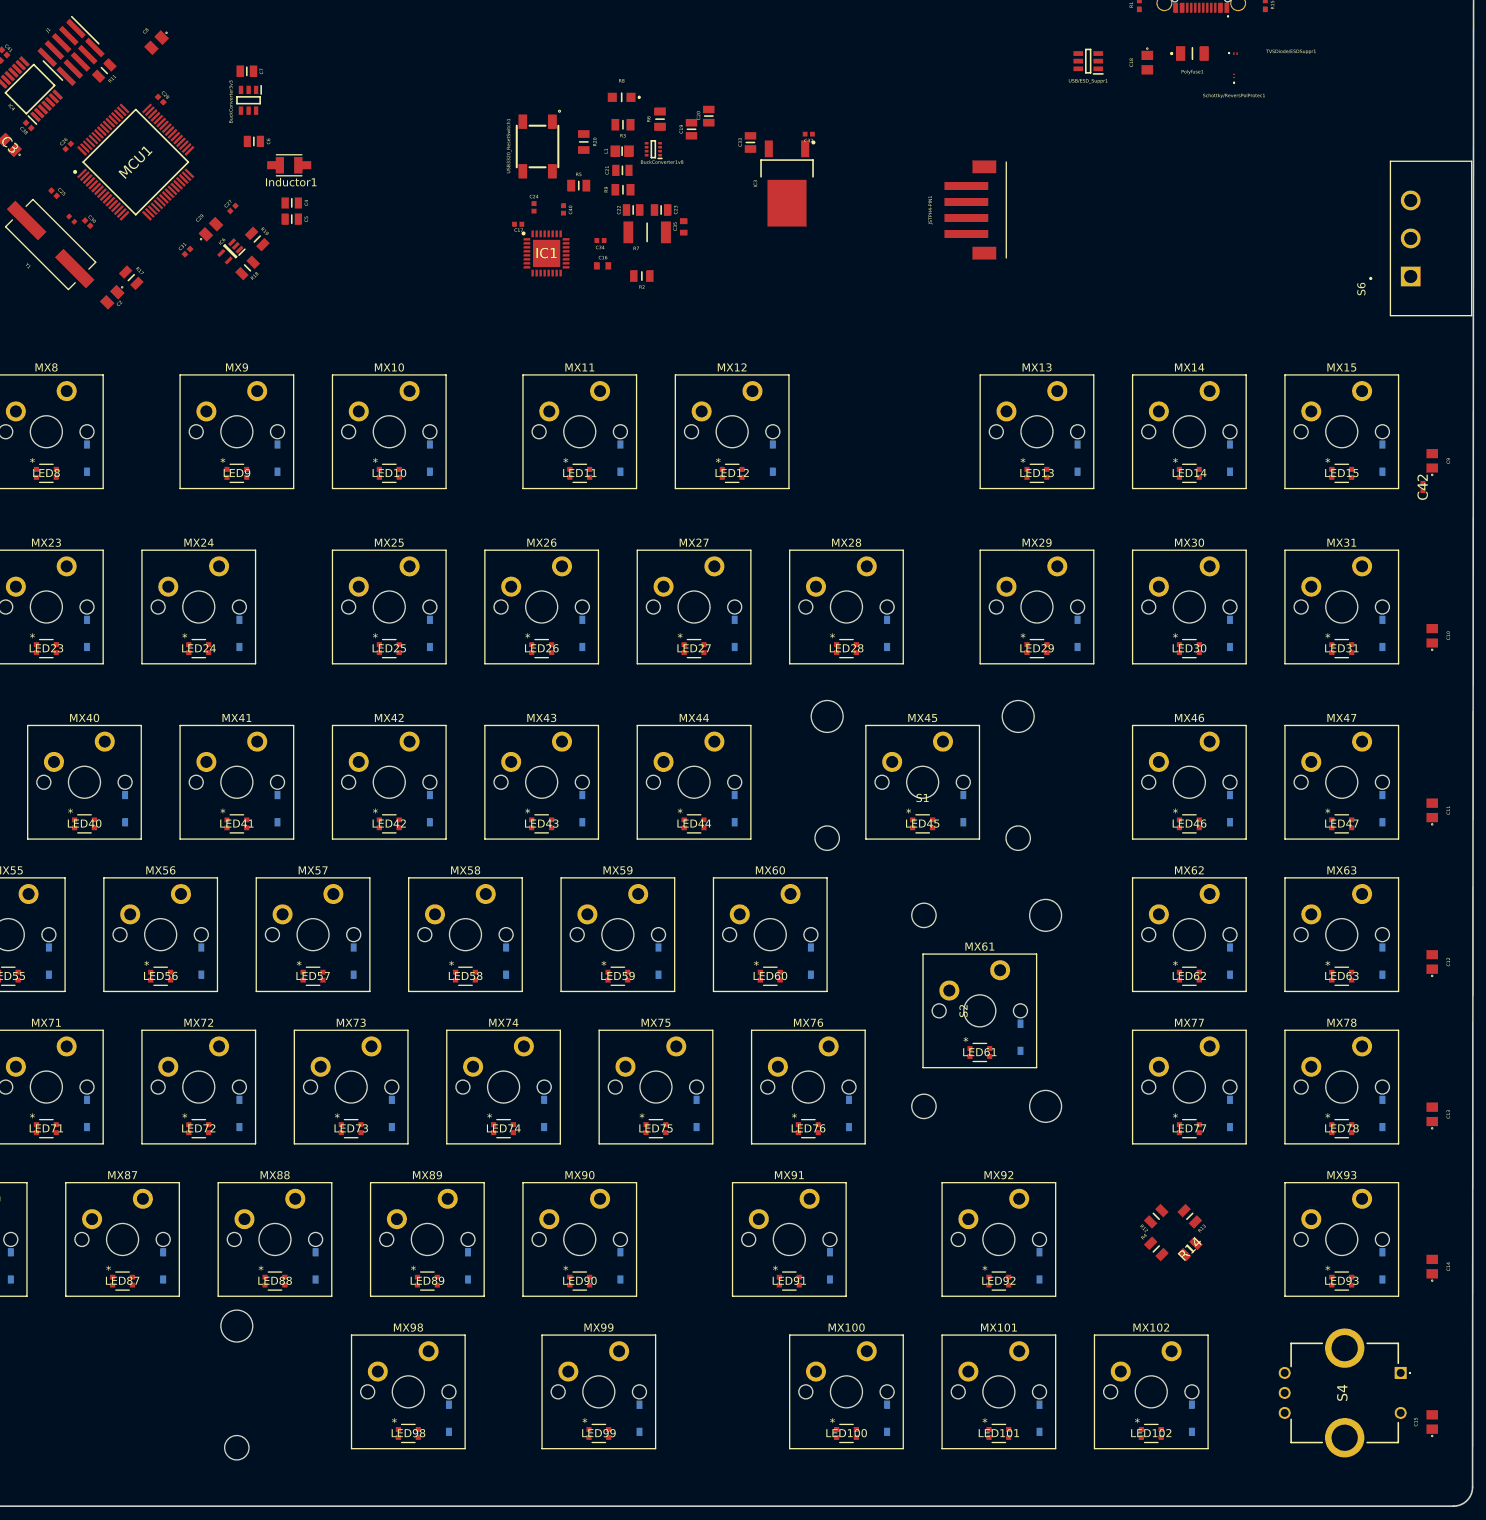
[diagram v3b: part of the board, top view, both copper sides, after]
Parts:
- removed Rotary_Encoder(30mm)1: PEC12R-4230F-S0024, SamacSys_Parts:PEC12R4230FS0024
- added S4: Rotary_Encoder(20mm), SamacSys_Parts:PEC12R3220FS0024, F.Cu at (374.4, 204.8)
- moved R4 37.3 mm to (343.8, 189.3), turned to 135 degrees
- moved R12 37.1 mm to (343.8, 185.2), turned to 45 degrees
- moved R13 36.6 mm to (348.0, 185.2), turned to 135 degrees
- moved R14 35.9 mm to (348.1, 189.3), turned to 45 degrees
- moved C15 28.8 mm to (378.3, 210.9)
- moved C25 7.83 mm to (206.1, 57.3)
- moved C35 3.93 mm to (284.8, 61.5), turned to 90 degrees
- moved C23 3.00 mm to (282.0, 59.4)
- moved R7 3.00 mm to (280.2, 62.2)
- moved C22 3.00 mm to (278.5, 59.4)
- moved R2 2.81 mm to (279.5, 67.7)
- moved C16 2.53 mm to (274.6, 66.4), turned to 0 degrees
- moved C34 2.23 mm to (274.4, 63.2), turned to 0 degrees
- moved R20 2.09 mm to (272.3, 50.9)
- moved C17 2.04 mm to (264.1, 61.2), turned to 180 degrees
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
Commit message: Fully Routed PCB
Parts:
- added H1: MountingHole, MountingHole:MountingHole_2.5mm_Pad_Via, F.Cu at (50.1, 34.4)
- added H2: MountingHole, MountingHole:MountingHole_2.5mm_Pad_Via, F.Cu at (50.1, 40.9)
- added H3: MountingHole, MountingHole:MountingHole_2.5mm_Pad_Via, F.Cu at (50.1, 47.5)
- added H4: MountingHole, MountingHole:MountingHole_2.5mm_Pad_Via, F.Cu at (50.1, 54.0)
- C1, C2: footprint SamacSys_Parts:C0805 -> SamacSys_Parts:C0603
- moved JSTPH4-PIN1 214.8 mm to (108.8, 55.7)
- moved R19 73.8 mm to (164.5, 32.0), turned to 45 degrees
- moved R18 68.8 mm to (168.7, 36.0)
- moved IC6 68.7 mm to (166.6, 34.0)
- moved R17 60.5 mm to (163.7, 37.0)
- moved C27 41.7 mm to (186.9, 55.6)
- moved PNPTransistor1 41.7 mm to (156.2, 38.0), turned to 135 degrees
- moved R16 41.3 mm to (154.4, 41.6), turned to -45 degrees
- moved C28 40.2 mm to (179.2, 44.8), turned to 135 degrees
- moved C31 39.8 mm to (183.0, 63.2), turned to -45 degrees
- moved C3 39.6 mm to (161.2, 56.4), turned to -135 degrees
- moved C41 39.1 mm to (218.5, 74.1), turned to 135 degrees
- moved C36 38.6 mm to (219.3, 73.4), turned to -45 degrees
- moved MCU1 38.3 mm to (178.0, 54.2)
- moved C26 38.3 mm to (169.6, 52.2)
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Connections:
- USB-C1 pad MH3: GND -> unconnected-(USB-C1-PadMH3)
- USB-C1 pad MH4: GND -> unconnected-(USB-C1-PadMH4)
- USB-C1 pad MH5: GND -> unconnected-(USB-C1-PadMH5)
- USB-C1 pad MH6: GND -> unconnected-(USB-C1-PadMH6)
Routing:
- net GND: track 0.00 -> 3407.9 mm, vias 0 -> 20
- net On/OffSwitch: track 0.00 -> 2465.8 mm
- net ROW3: track 0.00 -> 573.9 mm, vias 0 -> 9
- net ROW5: track 0.00 -> 573.7 mm, vias 0 -> 5
- net ROW4: track 0.00 -> 558.0 mm, vias 0 -> 8
- net ROW1: track 0.00 -> 537.3 mm, vias 0 -> 12
- net ROW2: track 0.00 -> 505.6 mm, vias 0 -> 11
- net ROW0: track 0.00 -> 471.3 mm, vias 0 -> 5
- net ROW6: track 0.00 -> 464.9 mm, vias 0 -> 3
- net +3.3V: track 0.00 -> 433.5 mm, vias 0 -> 8
- net +5V: track 0.00 -> 410.5 mm, vias 0 -> 8
- net COL16: track 0.00 -> 338.0 mm, vias 0 -> 2
- net COL12: track 0.00 -> 300.2 mm, vias 0 -> 2
- net COL9: track 0.00 -> 291.2 mm, vias 0 -> 2
- net COL1: track 0.00 -> 287.9 mm, vias 0 -> 2
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- removed copper zone on F.Cu, net GND

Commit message: Fixed DRC Errors
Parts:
- H1, H2, H3, H4: footprint MountingHole:MountingHole_2.5mm_Pad_Via -> MountingHole:MountingHole_2.5mm_Pad_TopBottom
- Schottky/ReversPolProtec1: value PMEG4005AESFYL -> PMEG10020ELRX; footprint SamacSys_Parts:PMEG4005AESFYL -> SamacSys_Parts:SODFL3517X110N
- TVSDiode/ESDSuppr1: value SP4337-01WTG -> PESD5V0C1BSFYL; footprint SamacSys_Parts:SP433701WTG -> SamacSys_Parts:PMEG3005AESFYL
- moved TVSDiode/ESDSuppr1 0.38 mm to (356.0, 40.2), turned to 90 degrees
- moved D72 0.22 mm to (229.2, 172.6)
- moved D70 0.18 mm to (191.1, 172.5)
- moved D71 0.18 mm to (210.2, 172.5)
- moved D74 0.18 mm to (267.3, 172.5)
- moved D75 0.18 mm to (286.4, 172.5)
- moved D13 0.18 mm to (334.0, 90.6)
- moved D15 0.18 mm to (372.1, 90.6)
- moved D2 0.18 mm to (81.6, 90.6)
- moved D6 0.18 mm to (167.3, 90.6)
- moved D7 0.18 mm to (191.1, 90.6)
- moved D9 0.18 mm to (234.0, 90.6)
- moved D100 0.18 mm to (310.2, 210.6)
- moved D101 0.18 mm to (329.2, 210.6)
- moved D33 0.18 mm to (81.6, 134.4)
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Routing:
- net ROW0: track 471.3 -> 474.2 mm
- net COL5: track 208.4 -> 210.4 mm
- net COL9: track 291.2 -> 292.7 mm
- net Net-(D63-A): track 10.6 -> 9.21 mm
- net Net-(D4-A): track 10.6 -> 9.23 mm
- net Net-(D28-A): track 10.6 -> 9.23 mm
- net Net-(D47-A): track 10.6 -> 9.24 mm
- net Net-(D2-A): track 10.6 -> 9.24 mm
- net Net-(LED88-DO): track 36.5 -> 35.2 mm
- net Net-(Schottky/ReversPolProtec1-A): track 8.89 -> 7.69 mm
- net ROW5: track 573.7 -> 574.8 mm
- net ROW4: track 558.0 -> 556.9 mm
- net Net-(LED53-DO): track 37.8 -> 38.9 mm
- net Net-(D8-A): track 8.13 -> 8.95 mm
- net ROW1: track 537.3 -> 536.5 mm
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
